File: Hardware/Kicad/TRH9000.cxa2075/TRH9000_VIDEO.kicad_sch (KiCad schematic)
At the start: 34 parts, among them J2 RGB, J3 Composite, J4 SVIDEO, Q1 BC817, U6 CXA2075M

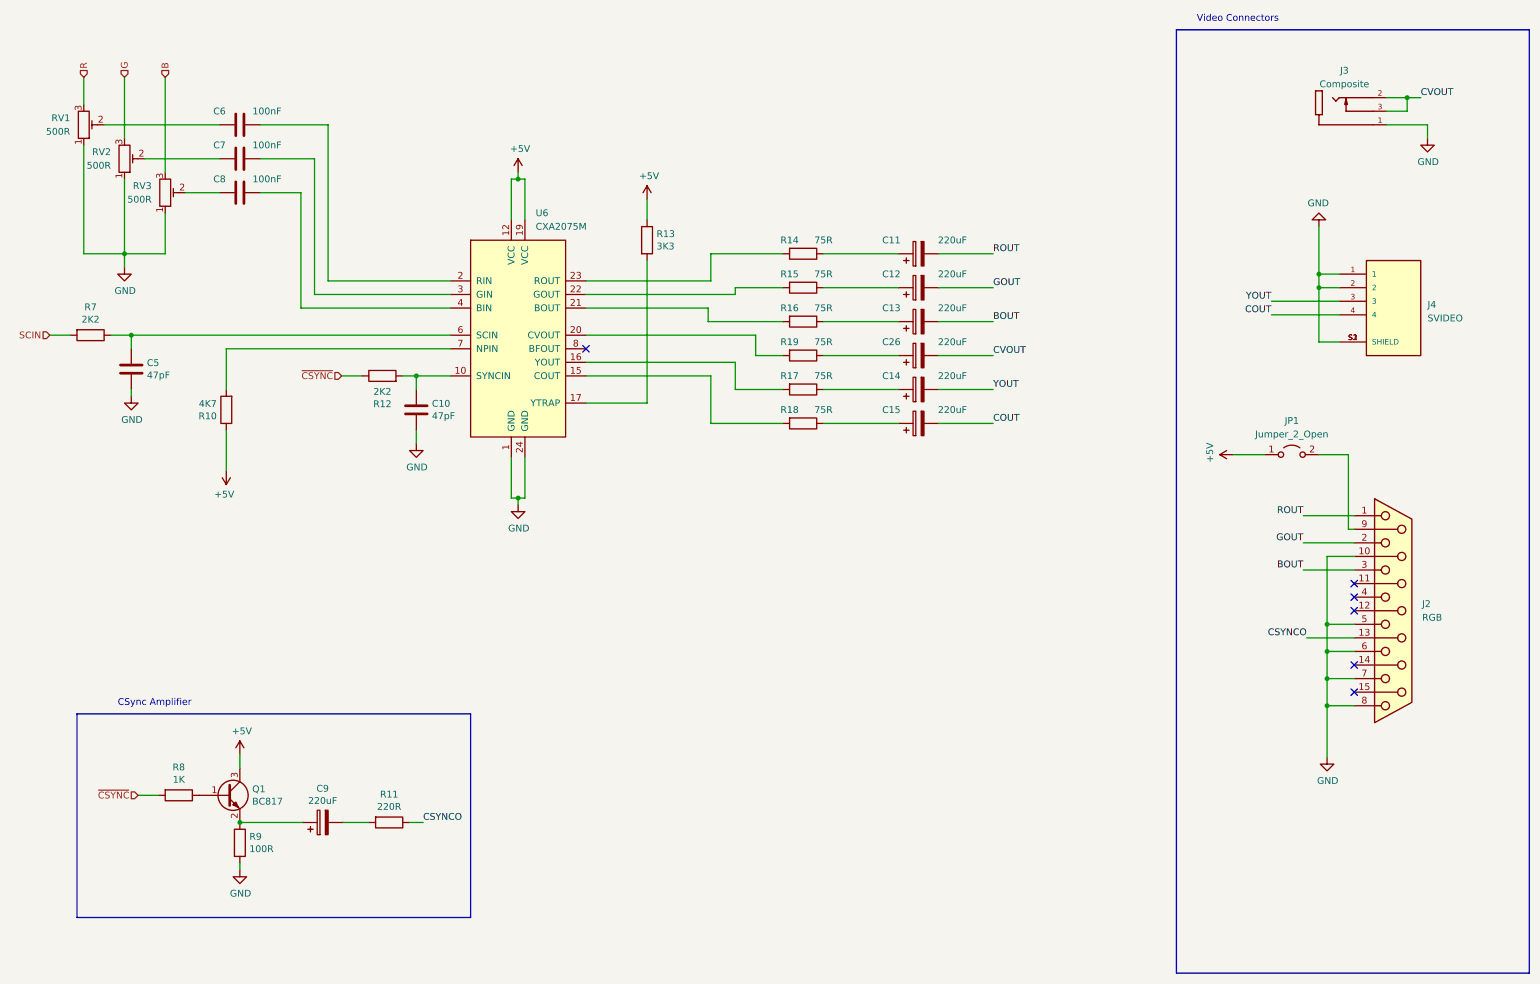
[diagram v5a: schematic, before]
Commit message: kicad 8 migration. minor positioning for the connectors
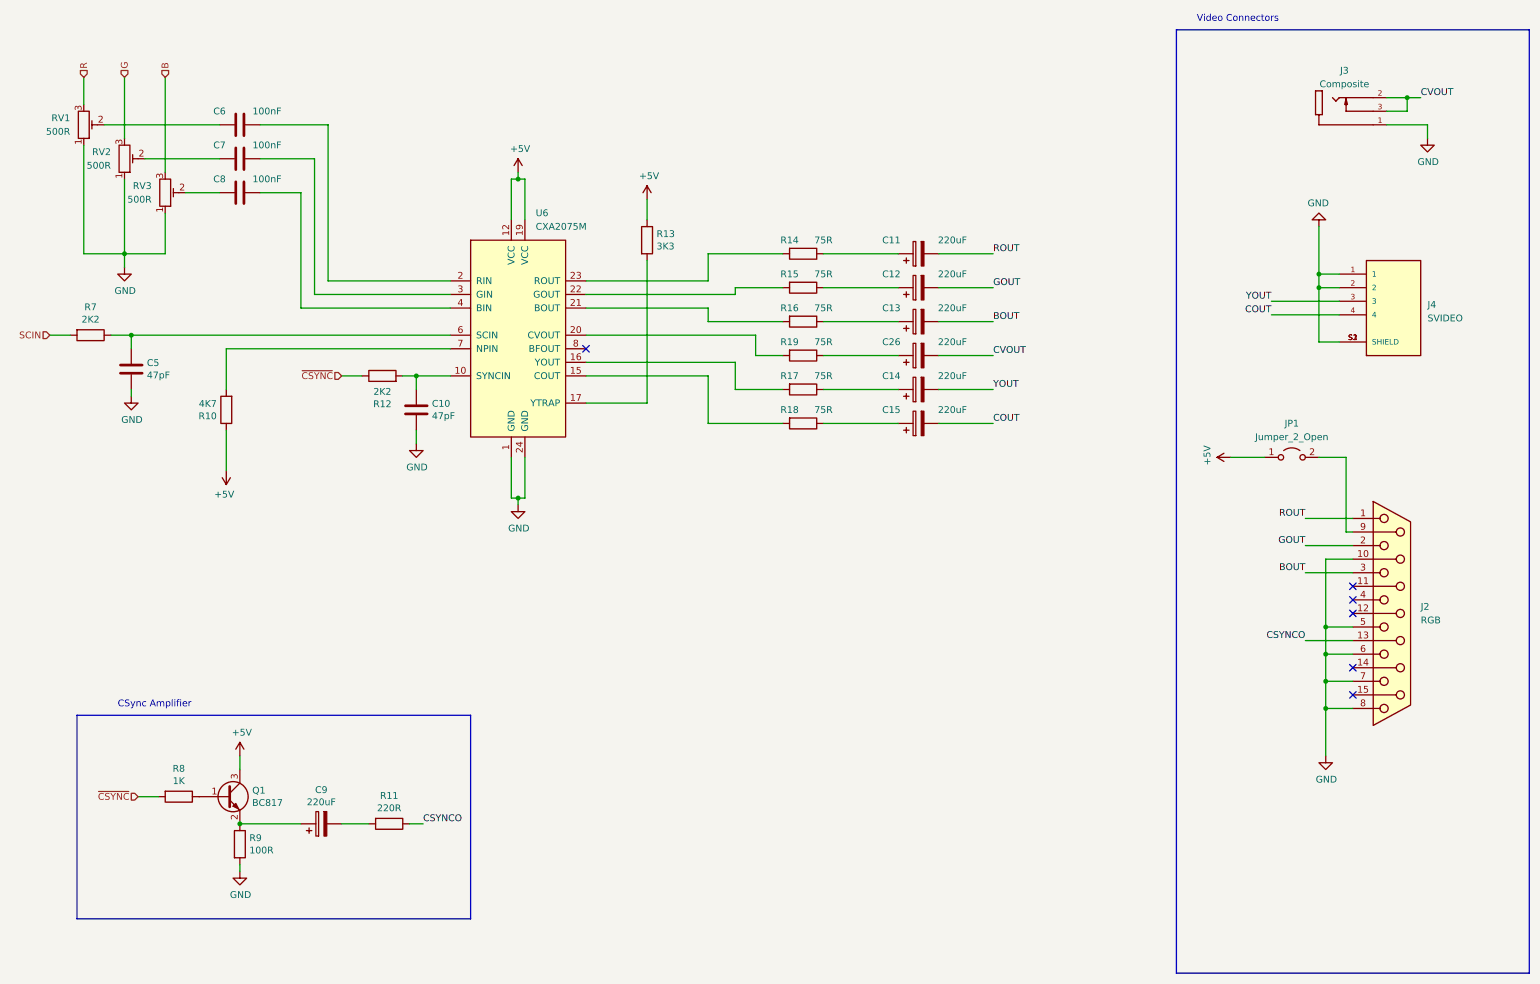
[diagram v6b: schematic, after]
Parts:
- J2: symbol Connector:DB15_Female -> Connector:DA15_Receptacle
- J3: footprint Footprints:SWITCHCRAFT_PJRAN1X1U02AUX -> PJRAN1X1U02AUX:SWITCHCRAFT_PJRAN1X1U02AUX; Description_1 (none) -> RCA Phono Connectors RCA PHONO JACK WHT.
- J4: footprint Footprints:CUI_MD-40SM -> MD-40SM:CUI_MD-40SM; Description_1 (none) -> 4 Pin, Mini Circular Connector w/ Shield
- U6: footprint Package_SO:SOP-24_7.5x15.4mm_P1.27mm -> Package_SO:SO-24_5.3x15mm_P1.27mm
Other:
- moved on the sheet: J2, JP1
